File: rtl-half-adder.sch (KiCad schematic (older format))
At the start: 75 parts, among them Q1 Q_NPN_EBC, Q10 Q_NPN_EBC, Q11 Q_NPN_EBC, Q12 Q_NPN_EBC, Q13 Q_NPN_EBC, Q14 Q_NPN_BEC, Q15 Q_NPN_BEC, Q16 Q_NPN_EBC, Q17 Q_NPN_BEC, Q18 Q_NPN_BEC, Q19 Q_NPN_EBC, Q2 Q_NPN_EBC, Q3 Q_NPN_EBC, Q4 Q_NPN_EBC, Q5 Q_NPN_EBC, Q6 Q_NPN_EBC, Q7 Q_NPN_EBC, Q8 Q_NPN_EBC, Q9 Q_NPN_EBC, SW1 SW_DIP_x02

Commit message: add link and datasheet for battery clip
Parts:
- BT?: Link (none) -> https://www.mouser.com/ProductDetail/BAT-HLD-012-THM
- D10, D11, D12, D13, D15, D3, D4, D5, D6: Link http://www.inolux-corp.com/datasheet/SMDLED/Mono%20Color%20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 -> https://www.mouser.com/ProductDetail/IN-S124BRUW
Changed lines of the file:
@@
 F 1 "LED" V 1397 3433 50  0000 R CNN
 F 2 "--Project:LED_1206_3216Metric_ReverseMount_Hole1.8x2.4mm" H 1450 3550 50  0001 C CNN
-F 3 "https://www.mouser.com/ProductDetail/IN-S124BRUW" H 1450 3550 50  0001 C CNN
-F 4 "http://www.inolux-corp.com/datasheet/SMDLED/Mono%20Color%20Reverse%20Mount/IN-S124BR%20Series_V1.0.pdf" H 0   0   50  0001 C CNN "Link"
+F 3 "http://www.inolux-corp.com/datasheet/SMDLED/Mono%20Color%20Reverse%20Mount/IN-S124BR%20Series_V1.0.pdf" H 1450 3550 50  0001 C CNN
+F 4 "https://www.mouser.com/ProductDetail/IN-S124BRUW" H 0   0   50  0001 C CNN "Link"
 	1    1450 3550
 	0    -1   -1   0
@@
 F 1 "LED" V 1747 3433 50  0000 R CNN
 F 2 "--Project:LED_1206_3216Metric_ReverseMount_Hole1.8x2.4mm" H 1800 3550 50  0001 C CNN
-F 3 "https://www.mouser.com/ProductDetail/IN-S124BRUW" H 1800 3550 50  0001 C CNN
-F 4 "http://www.inolux-corp.com/datasheet/SMDLED/Mono%20Color%20Reverse%20Mount/IN-S124BR%20Series_V1.0.pdf" H 0   0   50  0001 C CNN "Link"
+F 3 "http://www.inolux-corp.com/datasheet/SMDLED/Mono%20Color%20Reverse%20Mount/IN-S124BR%20Series_V1.0.pdf" H 1800 3550 50  0001 C CNN
+F 4 "https://www.mouser.com/ProductDetail/IN-S124BRUW" H 0   0   50  0001 C CNN "Link"
 	1    1800 3550
 	0    -1   -1   0
@@
 F 1 "LED" V 1397 5683 50  0000 R CNN
 F 2 "--Project:LED_1206_3216Metric_ReverseMount_Hole1.8x2.4mm" H 1450 5800 50  0001 C CNN
-F 3 "https://www.mouser.com/ProductDetail/IN-S124BRUW" H 1450 5800 50  0001 C CNN
-F 4 "http://www.inolux-corp.com/datasheet/SMDLED/Mono%20Color%20Reverse%20Mount/IN-S124BR%20Series_V1.0.pdf" H 0   0   50  0001 C CNN "Link"
+F 3 "http://www.inolux-corp.com/datasheet/SMDLED/Mono%20Color%20Reverse%20Mount/IN-S124BR%20Series_V1.0.pdf" H 1450 5800 50  0001 C CNN
+F 4 "https://www.mouser.com/ProductDetail/IN-S124BRUW" H 0   0   50  0001 C CNN "Link"
 	1    1450 5800
 	0    -1   -1   0
@@
 F 1 "LED" V 1747 5683 50  0000 R CNN
 F 2 "--Project:LED_1206_3216Metric_ReverseMount_Hole1.8x2.4mm" H 1800 5800 50  0001 C CNN
-F 3 "https://www.mouser.com/ProductDetail/IN-S124BRUW" H 1800 5800 50  0001 C CNN
-F 4 "http://www.inolux-corp.com/datasheet/SMDLED/Mono%20Color%20Reverse%20Mount/IN-S124BR%20Series_V1.0.pdf" H 0   0   50  0001 C CNN "Link"
+F 3 "http://www.inolux-corp.com/datasheet/SMDLED/Mono%20Color%20Reverse%20Mount/IN-S124BR%20Series_V1.0.pdf" H 1800 5800 50  0001 C CNN
+F 4 "https://www.mouser.com/ProductDetail/IN-S124BRUW" H 0   0   50  0001 C CNN "Link"
 	1    1800 5800
 	0    -1   -1   0
@@
 F 1 "LED" V 3197 5633 50  0000 R CNN
 F 2 "--Project:LED_1206_3216Metric_ReverseMount_Hole1.8x2.4mm" H 3250 5750 50  0001 C CNN
-F 3 "https://www.mouser.com/ProductDetail/IN-S124BRUW" H 3250 5750 50  0001 C CNN
-F 4 "http://www.inolux-corp.com/datasheet/SMDLED/Mono%20Color%20Reverse%20Mount/IN-S124BR%20Series_V1.0.pdf" H 0   0   50  0001 C CNN "Link"
+F 3 "http://www.inolux-corp.com/datasheet/SMDLED/Mono%20Color%20Reverse%20Mount/IN-S124BR%20Series_V1.0.pdf" H 3250 5750 50  0001 C CNN
+F 4 "https://www.mouser.com/ProductDetail/IN-S124BRUW" H 0   0   50  0001 C CNN "Link"
 	1    3250 5750
 	0    -1   -1   0
@@
 F 1 "LED" V 3547 5633 50  0000 R CNN
 F 2 "--Project:LED_1206_3216Metric_ReverseMount_Hole1.8x2.4mm" H 3600 5750 50  0001 C CNN
-F 3 "https://www.mouser.com/ProductDetail/IN-S124BRUW" H 3600 5750 50  0001 C CNN
-F 4 "http://www.inolux-corp.com/datasheet/SMDLED/Mono%20Color%20Reverse%20Mount/IN-S124BR%20Series_V1.0.pdf" H 0   0   50  0001 C CNN "Link"
+F 3 "http://www.inolux-corp.com/datasheet/SMDLED/Mono%20Color%20Reverse%20Mount/IN-S124BR%20Series_V1.0.pdf" H 3600 5750 50  0001 C CNN
+F 4 "https://www.mouser.com/ProductDetail/IN-S124BRUW" H 0   0   50  0001 C CNN "Link"
 	1    3600 5750
 	0    -1   -1   0
@@
 F 1 "LED" V 3197 3433 50  0000 R CNN
 F 2 "--Project:LED_1206_3216Metric_ReverseMount_Hole1.8x2.4mm" H 3250 3550 50  0001 C CNN
-F 3 "https://www.mouser.com/ProductDetail/IN-S124BRUW" H 3250 3550 50  0001 C CNN
-F 4 "http://www.inolux-corp.com/datasheet/SMDLED/Mono%20Color%20Reverse%20Mount/IN-S124BR%20Series_V1.0.pdf" H 0   0   50  0001 C CNN "Link"
+F 3 "http://www.inolux-corp.com/datasheet/SMDLED/Mono%20Color%20Reverse%20Mount/IN-S124BR%20Series_V1.0.pdf" H 3250 3550 50  0001 C CNN
+F 4 "https://www.mouser.com/ProductDetail/IN-S124BRUW" H 0   0   50  0001 C CNN "Link"
 	1    3250 3550
 	0    -1   -1   0
@@
 F 1 "LED" V 3547 3433 50  0000 R CNN
 F 2 "--Project:LED_1206_3216Metric_ReverseMount_Hole1.8x2.4mm" H 3600 3550 50  0001 C CNN
-F 3 "https://www.mouser.com/ProductDetail/IN-S124BRUW" H 3600 3550 50  0001 C CNN
-F 4 "http://www.inolux-corp.com/datasheet/SMDLED/Mono%20Color%20Reverse%20Mount/IN-S124BR%20Series_V1.0.pdf" H 0   0   50  0001 C CNN "Link"
+F 3 "http://www.inolux-corp.com/datasheet/SMDLED/Mono%20Color%20Reverse%20Mount/IN-S124BR%20Series_V1.0.pdf" H 3600 3550 50  0001 C CNN
+F 4 "https://www.mouser.com/ProductDetail/IN-S124BRUW" H 0   0   50  0001 C CNN "Link"
 	1    3600 3550
 	0    -1   -1   0
@@
 F 1 "LED" V 3897 3433 50  0000 R CNN
 F 2 "--Project:LED_1206_3216Metric_ReverseMount_Hole1.8x2.4mm" H 3950 3550 50  0001 C CNN
-F 3 "https://www.mouser.com/ProductDetail/IN-S124BRUW" H 3950 3550 50  0001 C CNN
-F 4 "http://www.inolux-corp.com/datasheet/SMDLED/Mono%20Color%20Reverse%20Mount/IN-S124BR%20Series_V1.0.pdf" H 0   0   50  0001 C CNN "Link"
+F 3 "http://www.inolux-corp.com/datasheet/SMDLED/Mono%20Color%20Reverse%20Mount/IN-S124BR%20Series_V1.0.pdf" H 3950 3550 50  0001 C CNN
+F 4 "https://www.mouser.com/ProductDetail/IN-S124BRUW" H 0   0   50  0001 C CNN "Link"
 	1    3950 3550
 	0    -1   -1   0
@@
 F 1 "Battery_Cell" H 5618 7105 50  0000 L CNN
 F 2 "--Project:BatteryHolder_CR1220_THT" V 5500 7160 50  0001 C CNN
-F 3 "~" V 5500 7160 50  0001 C CNN
+F 3 "https://linxtechnologies.com/wp/wp-content/uploads/bat-hld-012-thm.pdf" V 5500 7160 50  0001 C CNN
+F 4 "https://www.mouser.com/ProductDetail/BAT-HLD-012-THM" H 0   0   50  0001 C CNN "Link"
 	1    5500 7100
 	1    0    0    -1

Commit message: update schematic
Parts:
- removed D10, D11, D12, D13, D15, D3, D4, D5, D6: LED, --Project:LED_1206_3216Metric_ReverseMount_Hole1.8x2.4mm, symbol Device:LED
- removed Q14, Q15, Q17, Q18: Q_NPN_BEC, Package_TO_SOT_SMD:SOT-23_Handsoldering, symbol Device:Q_NPN_BEC
- removed R24, R25, R34, R35: 10k, Resistor_SMD:R_0805_2012Metric_Pad1.15x1.40mm_HandSolder, symbol Device:R_US
- removed R26, R27, R28, R29, R36, R37, R39, R40, R42: 68, Resistor_SMD:R_0805_2012Metric_Pad1.15x1.40mm_HandSolder, symbol Device:R_US
- removed SW?: SW_SPST, symbol Switch:SW_SPST
- added SW2: SW_SPDT, --Project:SW_EG1218_SPDT, symbol Switch:SW_SPDT
- gave numbers to parts that had none: 1
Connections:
- net VCC: now also SW2.2 (B)
- net CARRY_GATE: now reaches Q12.3 (C), R20.2
- net SUM_GATE: now reaches Q13.3 (C), R21.2
- net A_GATE: now reaches Q16.3 (C), R33.2
- net B_GATE: now reaches Q19.3 (C), R41.2
- net at BT1.1 (+): now also SW2.1 (A)
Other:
- moved on the sheet: BT1, D1, D14, D2, D9, Q1, Q10, Q11, Q12, Q13, Q16, Q19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

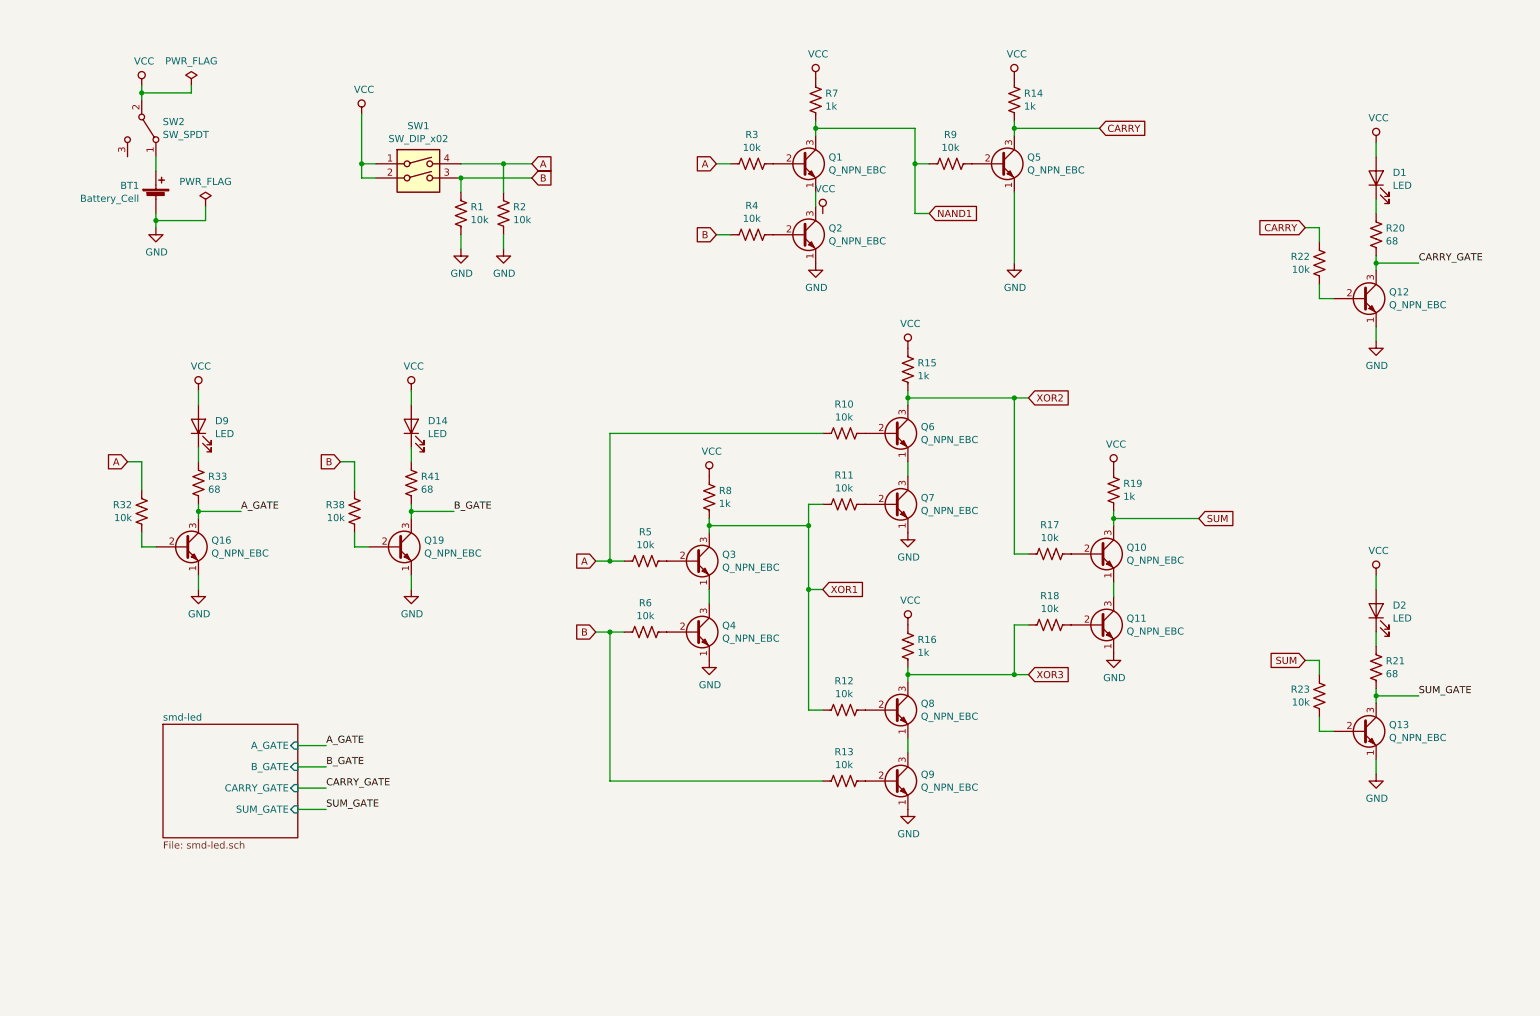
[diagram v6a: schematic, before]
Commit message: refactor numeric assignments
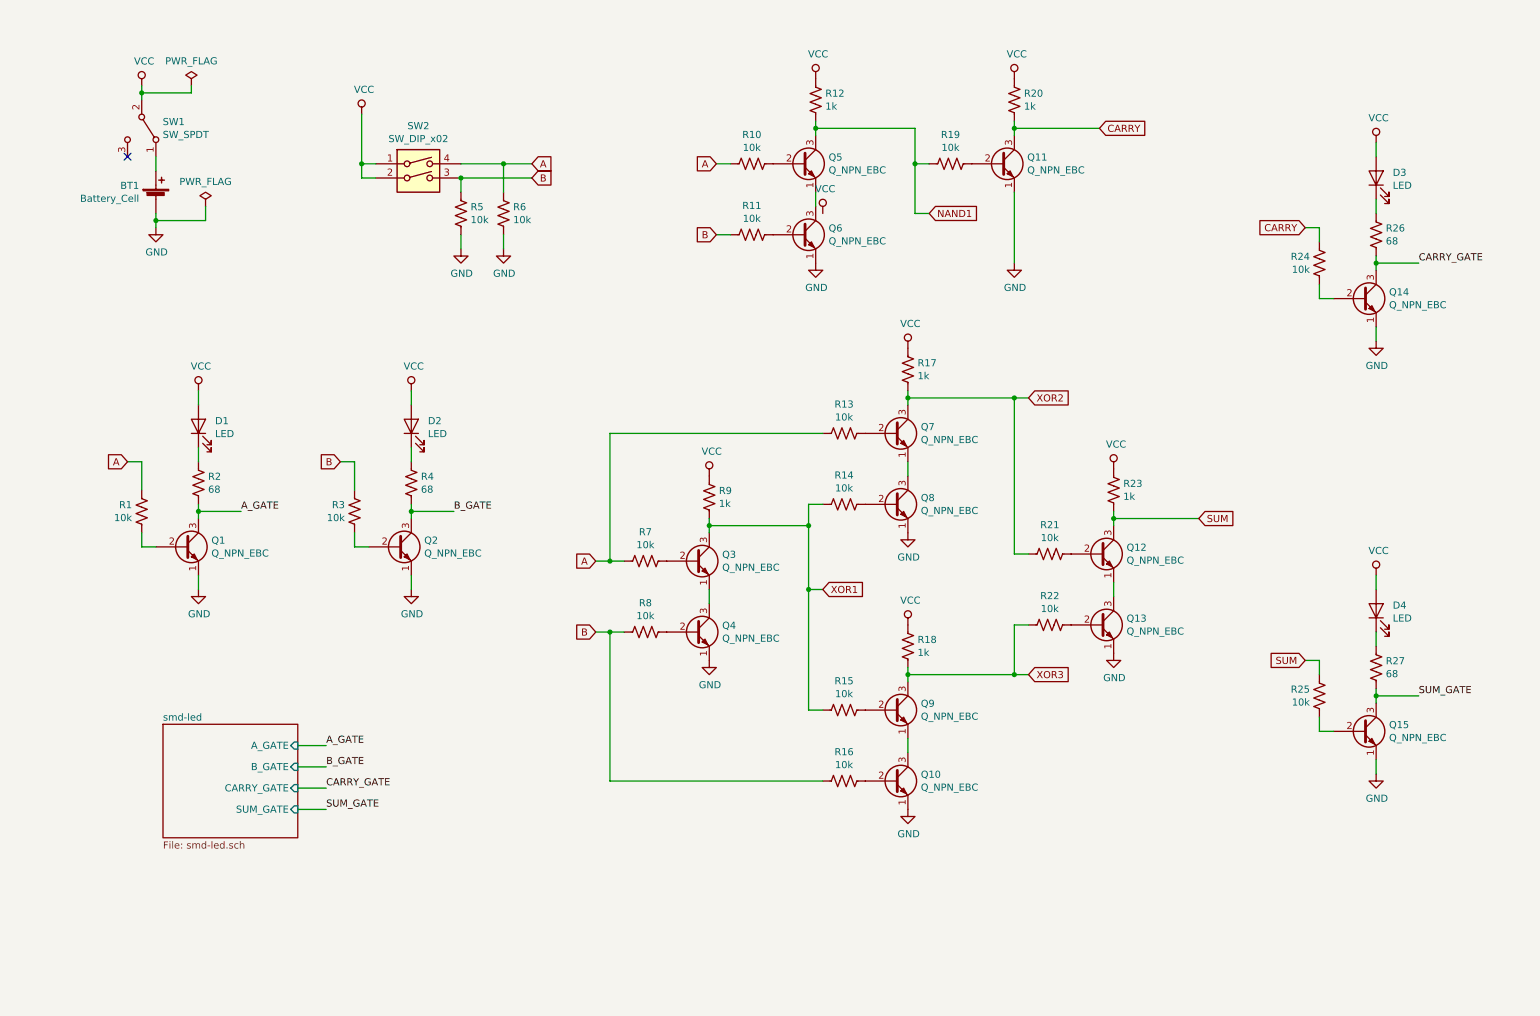
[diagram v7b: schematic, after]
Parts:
- renumbered D9 to D1, D14 to D2, D1 to D3, D2 to D4, Q16 to Q1, Q9 to Q10, Q5 to Q11, Q10 to Q12, Q11 to Q13, Q12 to Q14, Q13 to Q15, Q19 to Q2, Q1 to Q5, Q2 to Q6, Q6 to Q7, Q7 to Q8, Q8 to Q9, R32 to R1, R3 to R10, R4 to R11, R7 to R12, R10 to R13, R11 to R14, R12 to R15, R13 to R16, R15 to R17, R16 to R18, R9 to R19, R33 to R2, R14 to R20, R17 to R21, R18 to R22, R19 to R23, R22 to R24, R23 to R25, R20 to R26, R21 to R27, R38 to R3, R41 to R4, R1 to R5, R2 to R6, R5 to R7, R6 to R8, R8 to R9, SW2 to SW1, SW1 to SW2
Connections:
- no-connect marks 0 -> 1

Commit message: fix front fab layer
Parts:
- removed SW2: SW_DIP_x02, Button_Switch_THT:SW_DIP_SPSTx02_Slide_9.78x7.26mm_W7.62mm_P2.54mm, symbol Switch:SW_DIP_x02
- added SW2, SW3: SW_SPDT, --Project:SW_EG1218_SPDT, symbol Switch:SW_SPDT
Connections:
- net A: now also SW2.1 (A)
- net B: now also SW3.1 (A)
- net VCC: now also SW2.2 (B), SW3.2 (B)
- no-connect marks 1 -> 3
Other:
- moved on the sheet: R5, R6
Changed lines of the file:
@@
 Comment4 ""
 $EndDescr
-$Comp
-L Switch:SW_DIP_x02 SW2
-U 1 1 5CF808F6
-P 3350 1700
-F 0 "SW2" H 3350 2067 50  0000 C CNN
-F 1 "SW_DIP_x02" H 3350 1976 50  0000 C CNN
-F 2 "Button_Switch_THT:SW_DIP_SPSTx02_Slide_9.78x7.26mm_W7.62mm_P2.54mm" H 3350 1700 50  0001 C CNN
-F 3 "" H 3350 1700 50  0001 C CNN
-	1    3350 1700
-	1    0    0    -1
-$EndComp
-Wire Wire Line
-	2950 1250 2950 1600
-Wire Wire Line
-	2950 1600 3050 1600
-Wire Wire Line
-	3050 1700 2950 1700
-Wire Wire Line
-	2950 1700 2950 1600
-Connection ~ 2950 1600
+Wire Wire Line
+	3050 1850 2950 1850
 $Comp
 L Device:R_US R5
 U 1 1 5CF80AF3
-P 3650 1950
-F 0 "R5" H 3718 1996 50  0000 L CNN
-F 1 "10k" H 3718 1905 50  0000 L CNN
-F 2 "Resistor_THT:R_Axial_DIN0207_L6.3mm_D2.5mm_P7.62mm_Horizontal" V 3690 1940 50  0001 C CNN
-F 3 "~" H 3650 1950 50  0001 C CNN
-	1    3650 1950
+P 3650 2000
+F 0 "R5" H 3718 2046 50  0000 L CNN
+F 1 "10k" H 3718 1955 50  0000 L CNN
+F 2 "Resistor_THT:R_Axial_DIN0207_L6.3mm_D2.5mm_P7.62mm_Horizontal" V 3690 1990 50  0001 C CNN
+F 3 "~" H 3650 2000 50  0001 C CNN
+	1    3650 2000
 	1    0    0    -1
 $EndComp
@@
 L Device:R_US R6
 U 1 1 5CF80B47
-P 3950 1950
-F 0 "R6" H 4018 1996 50  0000 L CNN
-F 1 "10k" H 4018 1905 50  0000 L CNN
-F 2 "Resistor_THT:R_Axial_DIN0207_L6.3mm_D2.5mm_P7.62mm_Horizontal" V 3990 1940 50  0001 C CNN
-F 3 "~" H 3950 1950 50  0001 C CNN
-	1    3950 1950
+P 3950 2000
+F 0 "R6" H 4018 2046 50  0000 L CNN
+F 1 "10k" H 4018 1955 50  0000 L CNN
+F 2 "Resistor_THT:R_Axial_DIN0207_L6.3mm_D2.5mm_P7.62mm_Horizontal" V 3990 1990 50  0001 C CNN
+F 3 "~" H 3950 2000 50  0001 C CNN
+	1    3950 2000
 	1    0    0    -1
 $EndComp
@@
 L power:GND #PWR08
 U 1 1 5CF80BA4
-P 3650 2200
-F 0 "#PWR08" H 3650 1950 50  0001 C CNN
-F 1 "GND" H 3655 2027 50  0000 C CNN
-F 2 "" H 3650 2200 50  0001 C CNN
-F 3 "" H 3650 2200 50  0001 C CNN
-	1    3650 2200
-	1    0    0    -1
-$EndComp
-Wire Wire Line
-	3650 2100 3650 2200
+P 3650 2250
+F 0 "#PWR08" H 3650 2000 50  0001 C CNN
+F 1 "GND" H 3655 2077 50  0000 C CNN
+F 2 "" H 3650 2250 50  0001 C CNN
+F 3 "" H 3650 2250 50  0001 C CNN
+	1    3650 2250
+	1    0    0    -1
+$EndComp
+Wire Wire Line
+	3650 2150 3650 2250
 $Comp
 L power:VCC #PWR014
@@
 L power:VCC #PWR05
 U 1 1 5CF80A5A
-P 2950 1250
-F 0 "#PWR05" H 2950 1100 50  0001 C CNN
-F 1 "VCC" H 2967 1423 50  0000 C CNN
-F 2 "" H 2950 1250 50  0001 C CNN
-F 3 "" H 2950 1250 50  0001 C CNN
-	1    2950 1250
+P 2950 1100
+F 0 "#PWR05" H 2950 950 50  0001 C CNN
+F 1 "VCC" H 2967 1273 50  0000 C CNN
+F 2 "" H 2950 1100 50  0001 C CNN
+F 3 "" H 2950 1100 50  0001 C CNN
+	1    2950 1100
 	1    0    0    -1
 $EndComp
@@
 L power:GND #PWR09
 U 1 1 5CFEC196
-P 3950 2200
-F 0 "#PWR09" H 3950 1950 50  0001 C CNN
-F 1 "GND" H 3955 2027 50  0000 C CNN
-F 2 "" H 3950 2200 50  0001 C CNN
-F 3 "" H 3950 2200 50  0001 C CNN
-	1    3950 2200
-	1    0    0    -1
-$EndComp
-Wire Wire Line
-	3950 2100 3950 2200
-Text GLabel 4150 1600 2    50   Input ~ 0
+P 3950 2250
+F 0 "#PWR09" H 3950 2000 50  0001 C CNN
+F 1 "GND" H 3955 2077 50  0000 C CNN
+F 2 "" H 3950 2250 50  0001 C CNN
+F 3 "" H 3950 2250 50  0001 C CNN
+	1    3950 2250
+	1    0    0    -1
+$EndComp
+Wire Wire Line
+	3950 2150 3950 2250
+Text GLabel 4150 1200 2    50   Input ~ 0
 A
-Text GLabel 4150 1700 2    50   Input ~ 0
+Text GLabel 4150 1750 2    50   Input ~ 0
 B
 Text GLabel 5450 2100 0    50   Input ~ 0
@@
 	9700 5600 9800 5600
 Wire Wire Line
-	3650 1600 3950 1600
-Wire Wire Line
-	3650 1700 4150 1700
-Wire Wire Line
-	3650 1800 3650 1700
-Connection ~ 3650 1700
-Wire Wire Line
-	3950 1800 3950 1600
-Connection ~ 3950 1600
-Wire Wire Line
-	3950 1600 4150 1600
+	3450 1200 3950 1200
+Wire Wire Line
+	3650 1750 4150 1750
+Wire Wire Line
+	3650 1850 3650 1750
+Wire Wire Line
+	3950 1850 3950 1200
+Connection ~ 3950 1200
+Wire Wire Line
+	3950 1200 4150 1200
 Text GLabel 6200 4600 2    50   Input ~ 0
 XOR1
@@
 $EndComp
 NoConn ~ 1300 1550
+$Comp
+L Switch:SW_SPDT SW2
+U 1 1 5D043538
+P 3250 1300
+F 0 "SW2" H 3250 1585 50  0000 C CNN
+F 1 "SW_SPDT" H 3250 1494 50  0000 C CNN
+F 2 "--Project:SW_EG1218_SPDT" H 3250 1300 50  0001 C CNN
+F 3 "https://www.e-switch.com/system/asset/product_line/data_sheet/119/EG.pdf" H 3250 1300 50  0001 C CNN
+F 4 "https://www.mouser.com/ProductDetail/EG1218" H 1850 -50 50  0001 C CNN "Link"
+	1    3250 1300
+	1    0    0    -1
+$EndComp
+$Comp
+L Switch:SW_SPDT SW3
+U 1 1 5D0435E6
+P 3250 1850
+F 0 "SW3" H 3250 2135 50  0000 C CNN
+F 1 "SW_SPDT" H 3250 2044 50  0000 C CNN
+F 2 "--Project:SW_EG1218_SPDT" H 3250 1850 50  0001 C CNN
+F 3 "https://www.e-switch.com/system/asset/product_line/data_sheet/119/EG.pdf" H 3250 1850 50  0001 C CNN
+F 4 "https://www.mouser.com/ProductDetail/EG1218" H 1850 500 50  0001 C CNN "Link"
+	1    3250 1850
+	1    0    0    -1
+$EndComp
+Wire Wire Line
+	3650 1750 3450 1750
+Connection ~ 3650 1750
+Wire Wire Line
+	2950 1100 2950 1300
+Wire Wire Line
+	3050 1300 2950 1300
+Connection ~ 2950 1300
+Wire Wire Line
+	2950 1300 2950 1850
+NoConn ~ 3450 1400
+NoConn ~ 3450 1950
 $EndSCHEMATC
